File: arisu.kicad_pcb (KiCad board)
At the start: 2 copper layers, 373.1 x 140.4 mm, 122 parts, among them P1 USB_C_Plug_USB2.0, SW11 SW_Push, SW12 SW_Push, SW13 SW_Push, SW14 SW_Push, SW16 SW_Push, SW17 SW_Push, SW18 SW_Push, SW2 SW_Push, SW20 SW_Push, SW21 SW_Push, SW22 SW_Push, SW23 SW_Push, SW25 SW_Push, SW26 SW_Push, SW27 SW_Push, SW28 SW_Push, SW3 SW_Push, SW30 SW_Push, SW31 SW_Push, SW32 SW_Push, SW34 SW_Push, SW35 SW_Push, SW36 SW_Push, SW37 SW_Push, SW39 SW_Push, SW4 SW_Push, SW40 SW_Push, SW41 SW_Push, SW43 SW_Push, SW44 SW_Push, SW45 SW_Push, SW46 SW_Push, SW48 SW_Push, SW49 SW_Push, SW5 SW_Push, SW50 SW_Push, SW52 SW_Push, SW53 SW_Push, SW54 SW_Push, SW56 SW_Push, SW57 SW_Push, SW58 SW_Push, SW62 SW_Push, SW63 SW_Push, SW64 SW_Push, SW7 SW_Push, SW8 SW_Push, SW9 SW_Push, U1 USBLC6-2SC6, U2 ATmega32U4-AU, Y1 Crystal_GND24

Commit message: Almost finish initial routing and board edge cuts.
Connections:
- U2 pad 27: /col12 -> /col10
- U2 pad 29: /col10 -> /col12
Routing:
- net /col11: track 83.3 -> 259.0 mm, vias 0 -> 3
- net /col12: track 84.8 -> 255.3 mm, vias 0 -> 3
- net /col10: track 46.4 -> 194.8 mm, vias 0 -> 3
- net /col9: track 95.8 -> 195.7 mm, vias 0 -> 1
- net /row2: track 331.0 -> 400.2 mm, vias 1 -> 4
- net /row3: track 391.6 -> 430.4 mm, vias 1 -> 2
- net VCC: track 142.7 -> 168.4 mm, vias 8 -> 9
- net Net-(U2-Pad18): track 15.3 -> 0.00 mm, vias 1 -> 0
- net Net-(U2-Pad19): track 12.5 -> 0.00 mm, vias 1 -> 0
- net Net-(U2-Pad31): track 1.13 -> 0.00 mm
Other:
- board size 373.1 x 140.4 mm -> 372.8 x 133.5 mm

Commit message: Finish edge cuts.
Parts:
- moved H7 54.6 mm to (342.1, 70.6)
- moved H8 45.3 mm to (347.5, 124.7)
- moved H1 39.9 mm to (68.1, 58.9)
- moved H3 36.5 mm to (152.9, 66.5)
- moved H2 32.1 mm to (58.9, 122.9)
- moved H5 28.2 mm to (244.3, 66.8)
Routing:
- net GND: track 87.5 -> 89.4 mm, vias 11 -> 12
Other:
- board size 372.8 x 133.5 mm -> 330.8 x 110 mm
- board text added: "Ergaux 40-A 0.0.0 by FauxLearningMachine Based on Arisu by FateNozomi MIT Licensed"
- board text removed: "Faux Keebs Rev 0.0.0"
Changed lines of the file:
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@@
   (general
     (thickness 1.6)
-    (drawings 1393)
-    (tracks 1024)
+    (drawings 1395)
+    (tracks 1027)
     (zones 0)
     (modules 122)
@@
   )
   (module Mounting_Holes:MountingHole_2.2mm_M2_Pad (layer F.Cu)
-    (at 390.52664 110.72859)
+    (at 347.472 124.714)
     (descr "Mounting Hole 2.2mm, M2")
     (tags "mounting hole 2.2mm m2")
@@
   )
   (module Mounting_Holes:MountingHole_2.2mm_M2_Pad (layer F.Cu)
-    (at 32.512 40.894)
+    (at 68.072 58.928)
     (descr "Mounting Hole 2.2mm, M2")
     (tags "mounting hole 2.2mm m2")
@@
   )
   (module Mounting_Holes:MountingHole_2.2mm_M2_Pad (layer F.Cu)
-    (at 36.322 145.796)
+    (at 58.928 122.936)
     (descr "Mounting Hole 2.2mm, M2")
     (tags "mounting hole 2.2mm m2")
@@
   )
   (module Mounting_Holes:MountingHole_2.2mm_M2_Pad (layer F.Cu)
-    (at 128.58804 39.29079)
+    (at 152.908 66.548)
     (descr "Mounting Hole 2.2mm, M2")
     (tags "mounting hole 2.2mm m2")
@@
   )
   (module Mounting_Holes:MountingHole_2.2mm_M2_Pad (layer F.Cu)
-    (at 260.149165 43.410699)
+    (at 244.348 66.802)
     (descr "Mounting Hole 2.2mm, M2")
     (tags "mounting hole 2.2mm m2")
@@
   )
   (module Mounting_Holes:MountingHole_2.2mm_M2_Pad (layer F.Cu)
-    (at 390.52664 45.24394)
+    (at 342.138 70.612)
     (descr "Mounting Hole 2.2mm, M2")
     (tags "mounting hole 2.2mm m2")
@@
     (pad 1 thru_hole circle (at 0 0) (size 4.4 4.4) (drill 2.2) (layers *.Cu *.Mask))
   )
+  (gr_arc (start 223.774 156.225936) (end 224.028 158.225936) (angle 7.237817049) (layer Edge.Cuts) (width 0.15))
+  (gr_arc (start 358.934 129.032) (end 360.934 129.54) (angle 62.36092497) (layer Edge.Cuts) (width 0.15))
+  (gr_line (start 360.934 129.54) (end 371.169018 94.012472) (layer Edge.Cuts) (width 0.15))
+  (gr_arc (start 369.333585 93.218) (end 371.333585 93.218) (angle 23.40549348) (layer Edge.Cuts) (width 0.15))
+  (gr_line (start 371.333585 93.218) (end 371.221841 73.183163) (layer Edge.Cuts) (width 0.15))
+  (gr_arc (start 369.221841 73.098637) (end 371.221841 73.183163) (angle -23.15235932) (layer Edge.Cuts) (width 0.15))
+  (gr_line (start 363.17617 54.575219) (end 371.094 72.39) (layer Edge.Cuts) (width 0.15))
+  (gr_arc (start 361.17617 55.541474) (end 363.17617 54.575219) (angle -56.57547154) (layer Edge.Cuts) (width 0.15))
+  (gr_line (start 280.191398 48.26) (end 361.471398 53.34) (layer Edge.Cuts) (width 0.15))
   (gr_arc (start 173.482 156.4236) (end 172.974 158.1696) (angle -16.22239404) (layer Edge.Cuts) (width 0.15))
   (gr_arc (start 55.372 130.266934) (end 53.594 131.758934) (angle -37.58167884) (layer Edge.Cuts) (width 0.15))
@@
   (gr_arc (start 41.589725 92.605503) (end 40.560256 92.676119) (angle 26.94287593) (layer Edge.Cuts) (width 0.15))
   (gr_line (start 62.231355 53.130208) (end 116.84 48.26) (layer Edge.Cuts) (width 0.15))
-  (gr_line (start 246.38 49.53) (end 280.162 48.26) (layer Edge.Cuts) (width 0.15))
+  (gr_line (start 246.38 49.53) (end 280.191398 48.26) (layer Edge.Cuts) (width 0.15))
   (gr_line (start 116.84 48.26) (end 150.622 49.53) (layer Edge.Cuts) (width 0.15))
   (gr_line (start 206.756 73.914) (end 246.38 49.53) (layer Edge.Cuts) (width 0.15))
   (gr_line (start 190.246 73.914) (end 206.756 73.914) (layer Edge.Cuts) (width 0.15))
   (gr_line (start 150.622 49.53) (end 190.246 73.914) (layer Edge.Cuts) (width 0.15))
-  (gr_line (start 27.4125 34.90953) (end 396.47979 34.90953) (layer Edge.Cuts) (width 0.15))
-  (gr_arc (start 396.47979 36.90953) (end 398.47979 36.90953) (angle -90) (layer Edge.Cuts) (width 0.15))
-  (gr_line (start 82.296 157.734) (end 29.93629 157.734) (layer Edge.Cuts) (width 0.15))
   (gr_line (start 54.872921 132.533709) (end 172.974 158.1696) (layer Edge.Cuts) (width 0.15))
-  (gr_line (start 398.47979 36.90953) (end 398.47979 117.87237) (layer Edge.Cuts) (width 0.15))
-  (gr_arc (start 391.668 157.512) (end 393.668 157.512) (angle 90) (layer Edge.Cuts) (width 0.15))
   (gr_line (start 84.24337 63.547863) (end 84.012299 63.192045) (layer Eco2.User) (width 0.2))
   (gr_line (start 124.065742 58.006322) (end 124.42156 57.775252) (layer Eco2.User) (width 0.2))
@@
   (gr_line (start 40.34 32.02) (end 40.64 31.72) (layer Eco2.User) (width 0.2))
   (gr_line (start 40.64 45.72) (end 40.34 45.42) (layer Eco2.User) (width 0.2))
-  (gr_text "Faux Keebs Rev 0.0.0" (at 335.026 155.702) (layer B.SilkS)
+  (gr_text "Ergaux 40-A 0.0.0 by FauxLearningMachine\nBased on Arisu by FateNozomi\nMIT Licensed" (at 131.318 122.174 -12) (layer B.SilkS)
     (effects (font (size 1.5 1.5) (thickness 0.3)) (justify mirror))
   )
   (gr_arc (start 62.441524 55.023615) (end 60.695524 54.261615) (angle 60.08835891) (layer Edge.Cuts) (width 0.15))
-  (gr_arc (start 27.686 155.48) (end 25.686 155.48) (angle -90) (layer Edge.Cuts) (width 0.15))
-  (gr_line (start 228.092 158.242) (end 353.822 133.604) (layer Edge.Cuts) (width 0.15))
+  (gr_line (start 224.028 158.225936) (end 359.41177 131.039436) (layer Edge.Cuts) (width 0.15))
   (gr_line (start 173.482 158.242) (end 223.774 158.242) (layer Edge.Cuts) (width 0.15))
-  (gr_line (start 386.334 168.402) (end 319.65872 168.402) (layer Edge.Cuts) (width 0.15))
   (gr_line (start 60.695524 54.261615) (end 40.64 92.202) (layer Edge.Cuts) (width 0.15))
   (via (at 180.086 109.728) (size 0.8) (drill 0.4) (layers F.Cu B.Cu) (net 1))
@@
   (segment (start 207.38438 99.49367) (end 207.38438 100.71762) (width 0.375) (layer B.Cu) (net 1))
   (segment (start 207.38438 100.71762) (end 207.264 100.838) (width 0.375) (layer B.Cu) (net 1))
+  (via (at 192.024 109.728) (size 0.8) (drill 0.4) (layers F.Cu B.Cu) (net 1))
+  (segment (start 191.93849 107.8063) (end 191.93849 109.64249) (width 0.375) (layer B.Cu) (net 1))
+  (segment (start 191.93849 109.64249) (end 192.024 109.728) (width 0.375) (layer B.Cu) (net 1))
   (via (at 198.374 85.09) (size 0.8) (drill 0.4) (layers F.Cu B.Cu) (net 2))
   (via (at 189.77405 117.602) (size 0.8) (drill 0.4) (layers F.Cu B.Cu) (net 2))

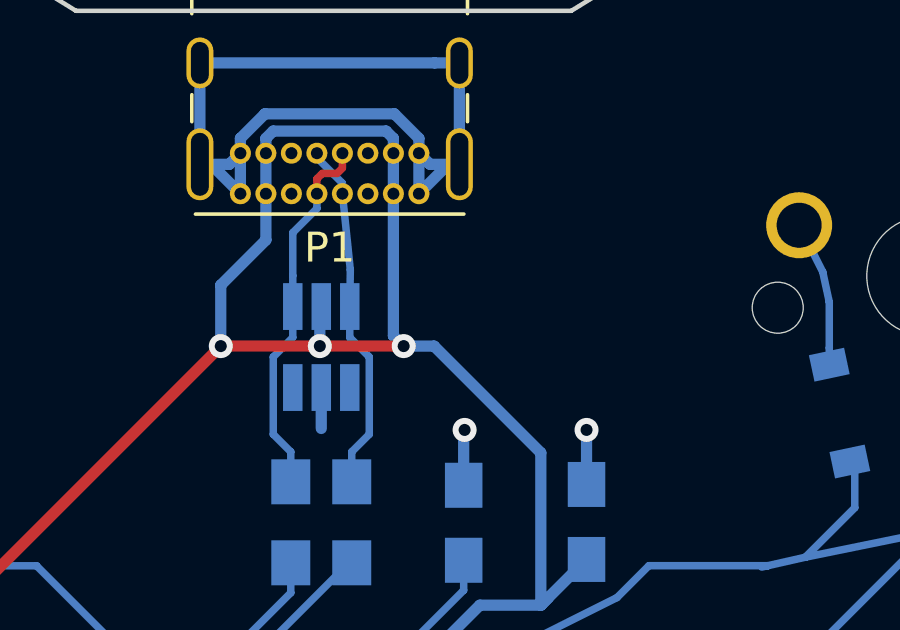
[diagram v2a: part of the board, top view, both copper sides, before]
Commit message: Fix missing connection to ground on ESD module.
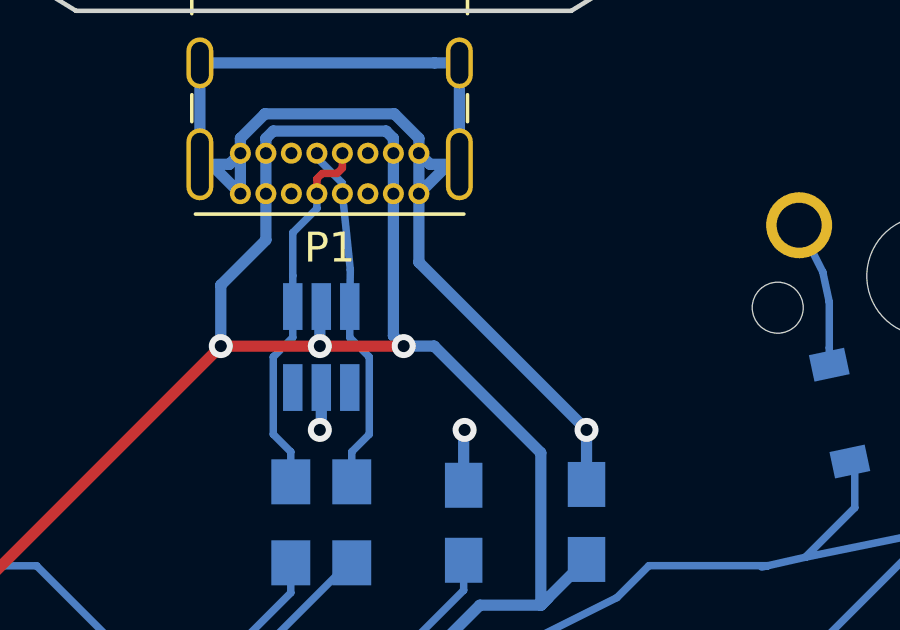
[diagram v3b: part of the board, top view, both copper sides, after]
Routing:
- net GND: track 89.4 -> 99.7 mm, vias 12 -> 13
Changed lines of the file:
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@@
     (thickness 1.6)
     (drawings 1395)
-    (tracks 1027)
+    (tracks 1031)
     (zones 0)
     (modules 122)
@@
   (segment (start 187.03849 110.3063) (end 188.905702 110.3063) (width 0.375) (layer B.Cu) (net 1))
   (segment (start 181.85649 107.6643) (end 180.1177 107.6643) (width 0.375) (layer B.Cu) (net 1))
-  (segment (start 198.42167 86.47162) (end 198.42167 87.83633) (width 0.375) (layer B.Cu) (net 1))
   (segment (start 180.1177 107.6643) (end 180.086 107.696) (width 0.375) (layer B.Cu) (net 1))
   (segment (start 187.03849 116.7063) (end 188.16349 116.7063) (width 0.375) (layer B.Cu) (net 1))
@@
   (segment (start 191.93849 107.8063) (end 191.93849 109.64249) (width 0.375) (layer B.Cu) (net 1))
   (segment (start 191.93849 109.64249) (end 192.024 109.728) (width 0.375) (layer B.Cu) (net 1))
+  (via (at 198.374 87.884) (size 0.8) (drill 0.4) (layers F.Cu B.Cu) (net 1))
+  (segment (start 198.42167 86.47162) (end 198.42167 87.83633) (width 0.375) (layer B.Cu) (net 1))
+  (segment (start 198.42167 87.83633) (end 198.374 87.884) (width 0.375) (layer B.Cu) (net 1))
+  (segment (start 201.676 82.296) (end 207.264 87.884) (width 0.375) (layer B.Cu) (net 1))
+  (segment (start 201.676 80.01) (end 201.676 82.296) (width 0.375) (layer B.Cu) (net 1))
   (via (at 198.374 85.09) (size 0.8) (drill 0.4) (layers F.Cu B.Cu) (net 2))
   (via (at 189.77405 117.602) (size 0.8) (drill 0.4) (layers F.Cu B.Cu) (net 2))

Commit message: Finalize PCB design for round 1.
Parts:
- removed D64: D, Diode_SMD:D_SOD-123
- removed SW64: SW_Push, MX_Switch:SW_Cherry_MX_1.00u_PCB
- SW57: footprint MX_Switch:SW_Cherry_MX_2.25u_PCB_ReversedStabilizers -> MX_Switch:SW_Cherry_MX_1.75u_PCB
- moved D57 4.72 mm to (341.1, 87.4)
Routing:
- net /row3: track 430.4 -> 345.9 mm
- net /col11: track 259.0 -> 222.9 mm
- net /row1: track 399.1 -> 391.9 mm
- net Net-(D64-Pad2): track 4.47 -> 0.00 mm
- net /col12: track 255.3 -> 256.1 mm
- net Net-(D57-Pad2): track 4.76 -> 4.20 mm
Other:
- board size 330.8 x 110 mm -> 331.1 x 106.2 mm
